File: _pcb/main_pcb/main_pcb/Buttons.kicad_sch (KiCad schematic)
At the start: 9 parts, among them SW1 SW_Push, SW2 SW_Push, SW3 SW_Push, SW4 SW_Push, SW5 SW_Push, SW6 SW_Push, SW7 SW_Push, SW8 SW_Push, U3 PCF8575DBR

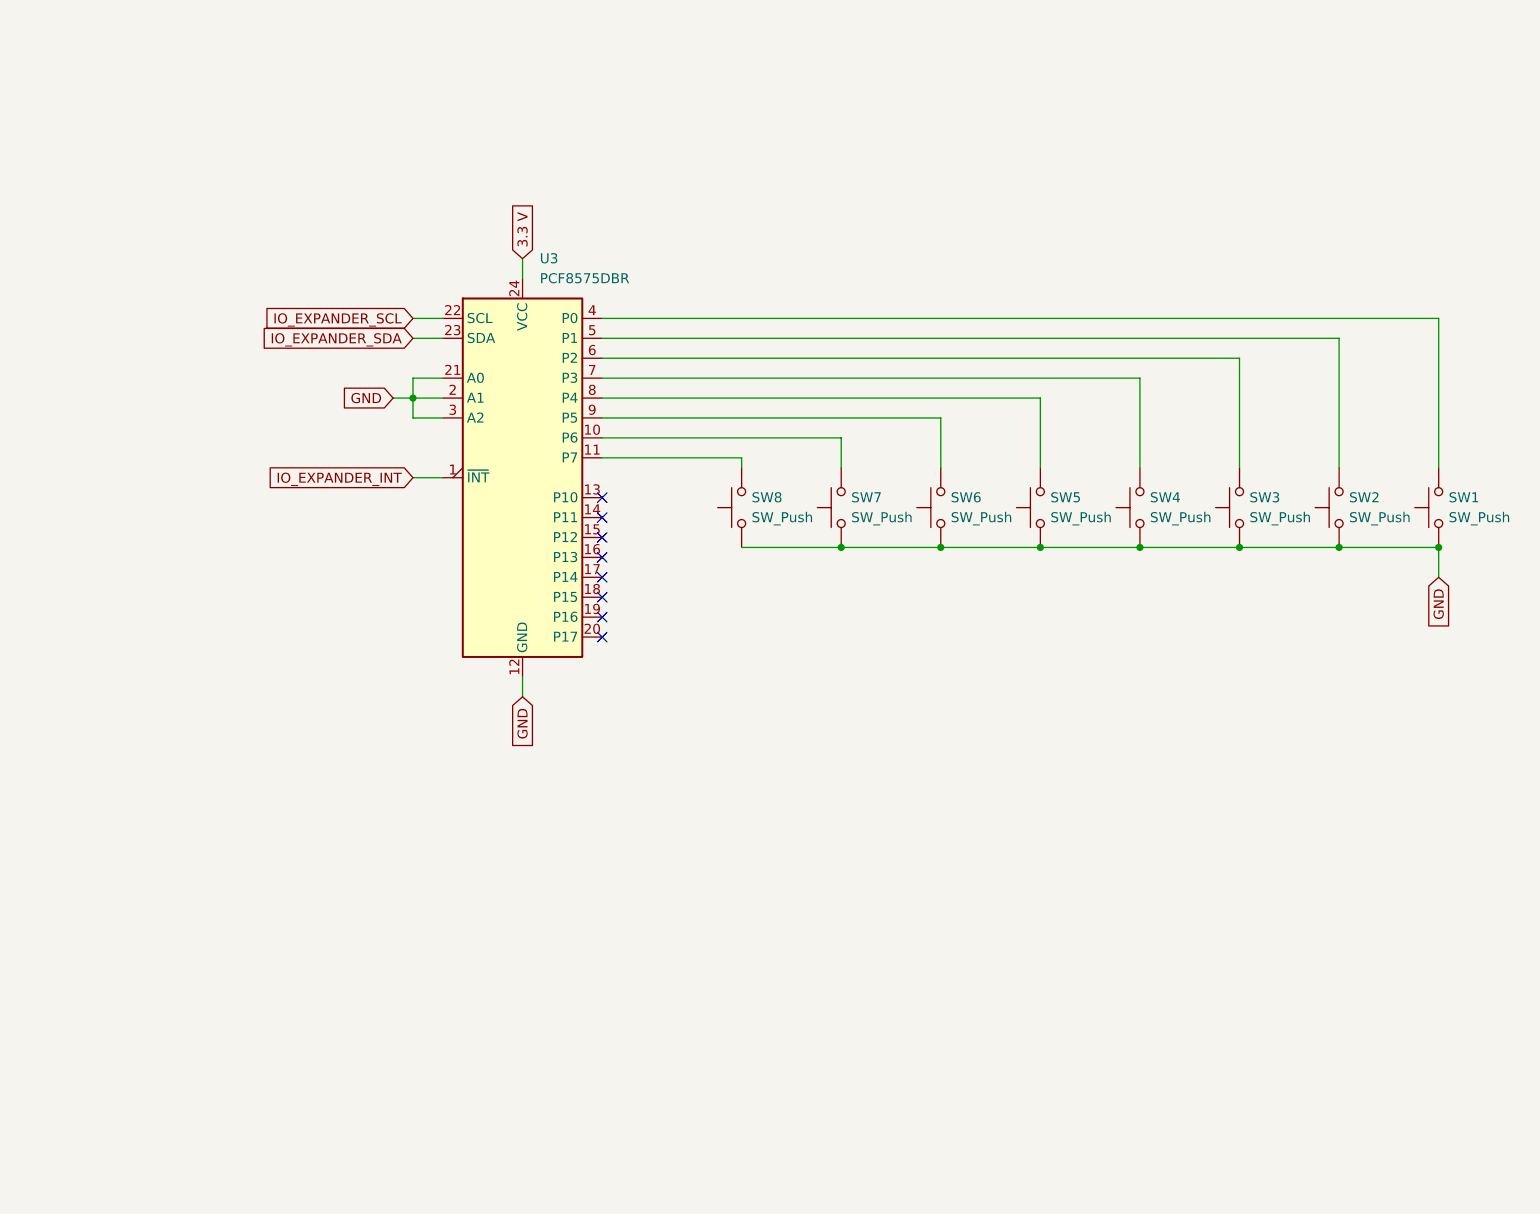
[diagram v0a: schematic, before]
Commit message: added leds to io expander
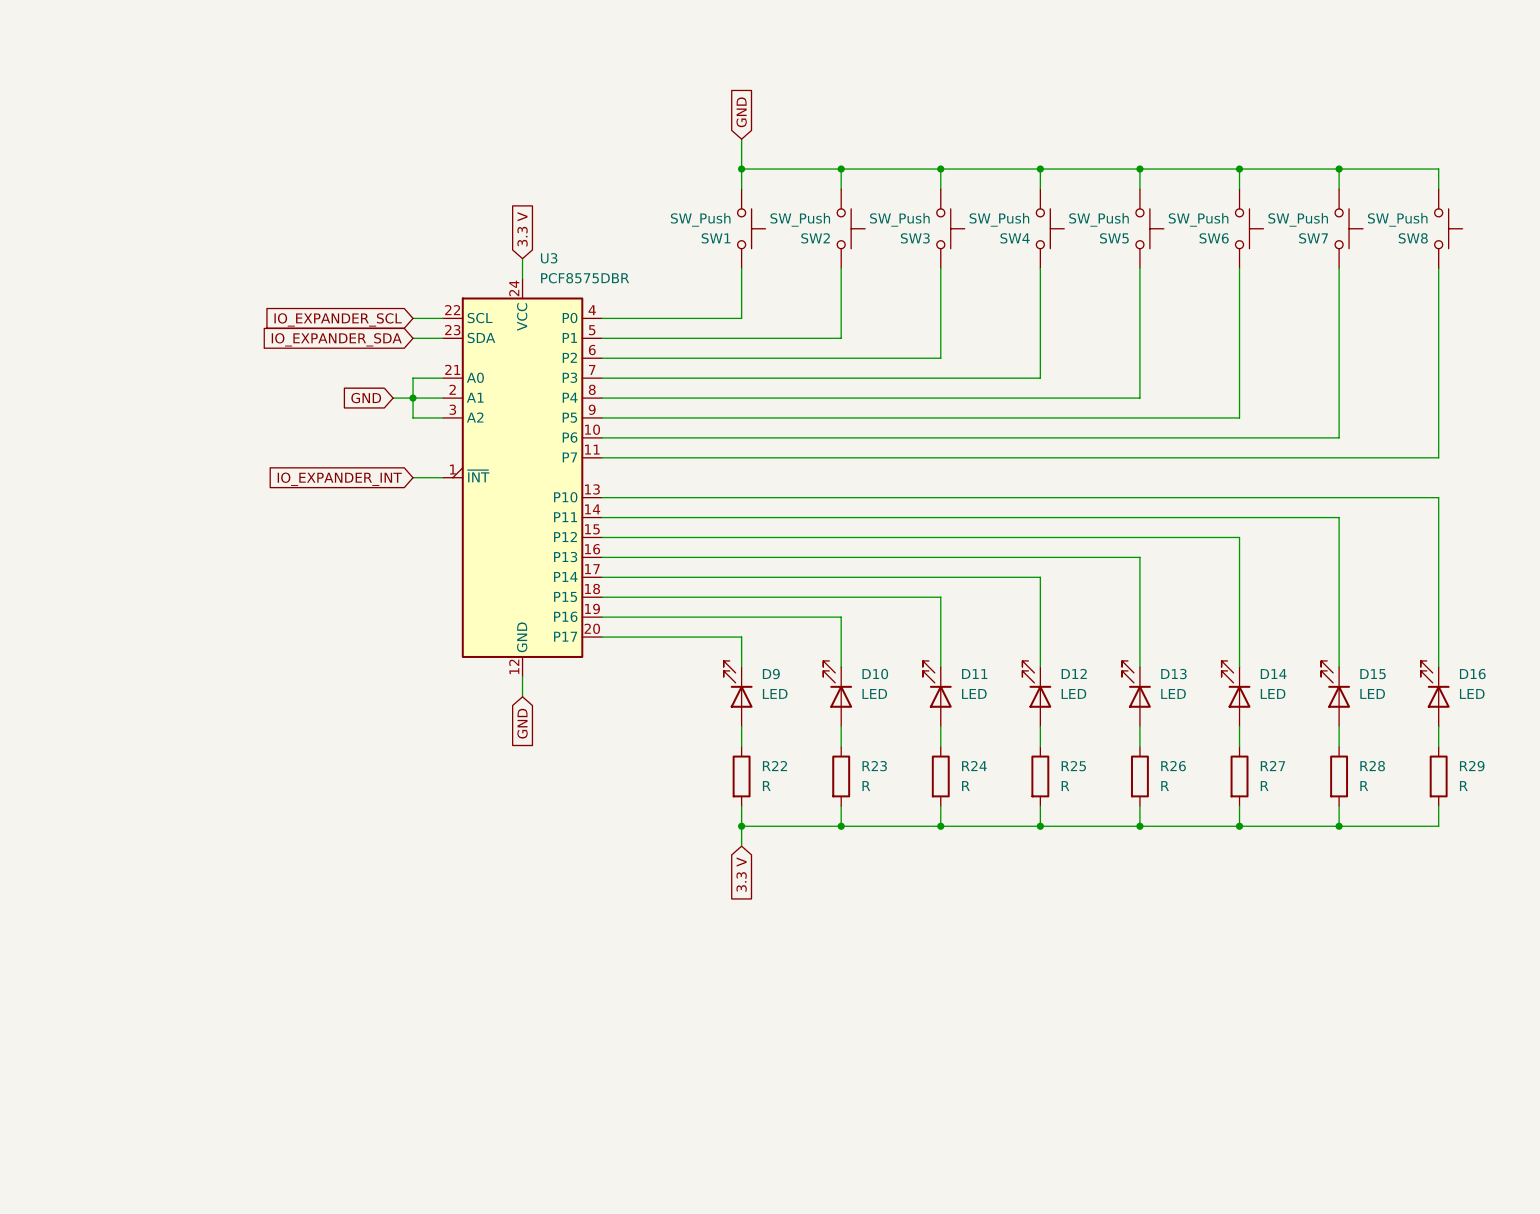
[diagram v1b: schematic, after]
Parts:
- added D10, D11, D12, D13, D14, D15, D16, D9: LED, symbol Device:LED
- added R22, R23, R24, R25, R26, R27, R28, R29: R, symbol Device:R
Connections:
- net 3.3 V: now also R22.2, R23.2, R24.2, R25.2, R26.2, R27.2, R28.2, R29.2
- net at U3.13 (P10): now also D16.1 (K)
- net at U3.14 (P11): now also D15.1 (K)
- net at U3.15 (P12): now also D14.1 (K)
- net at U3.16 (P13): now also D13.1 (K)
- net at U3.17 (P14): now also D12.1 (K)
- net at U3.18 (P15): now also D11.1 (K)
- net at U3.19 (P16): now also D10.1 (K)
- net at U3.20 (P17): now also D9.1 (K)
- new net: D12.2 (A), R25.1
- new net: D9.2 (A), R22.1
- new net: D14.2 (A), R27.1
- new net: D10.2 (A), R23.1
- new net: D13.2 (A), R26.1
- new net: D11.2 (A), R24.1
- new net: D16.2 (A), R29.1
- new net: D15.2 (A), R28.1
- no-connect marks 8 -> 0
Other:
- moved on the sheet: SW1, SW2, SW3, SW4, SW5, SW6, SW7, SW8

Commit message: moved to two pcf8574 instead of pcf8575
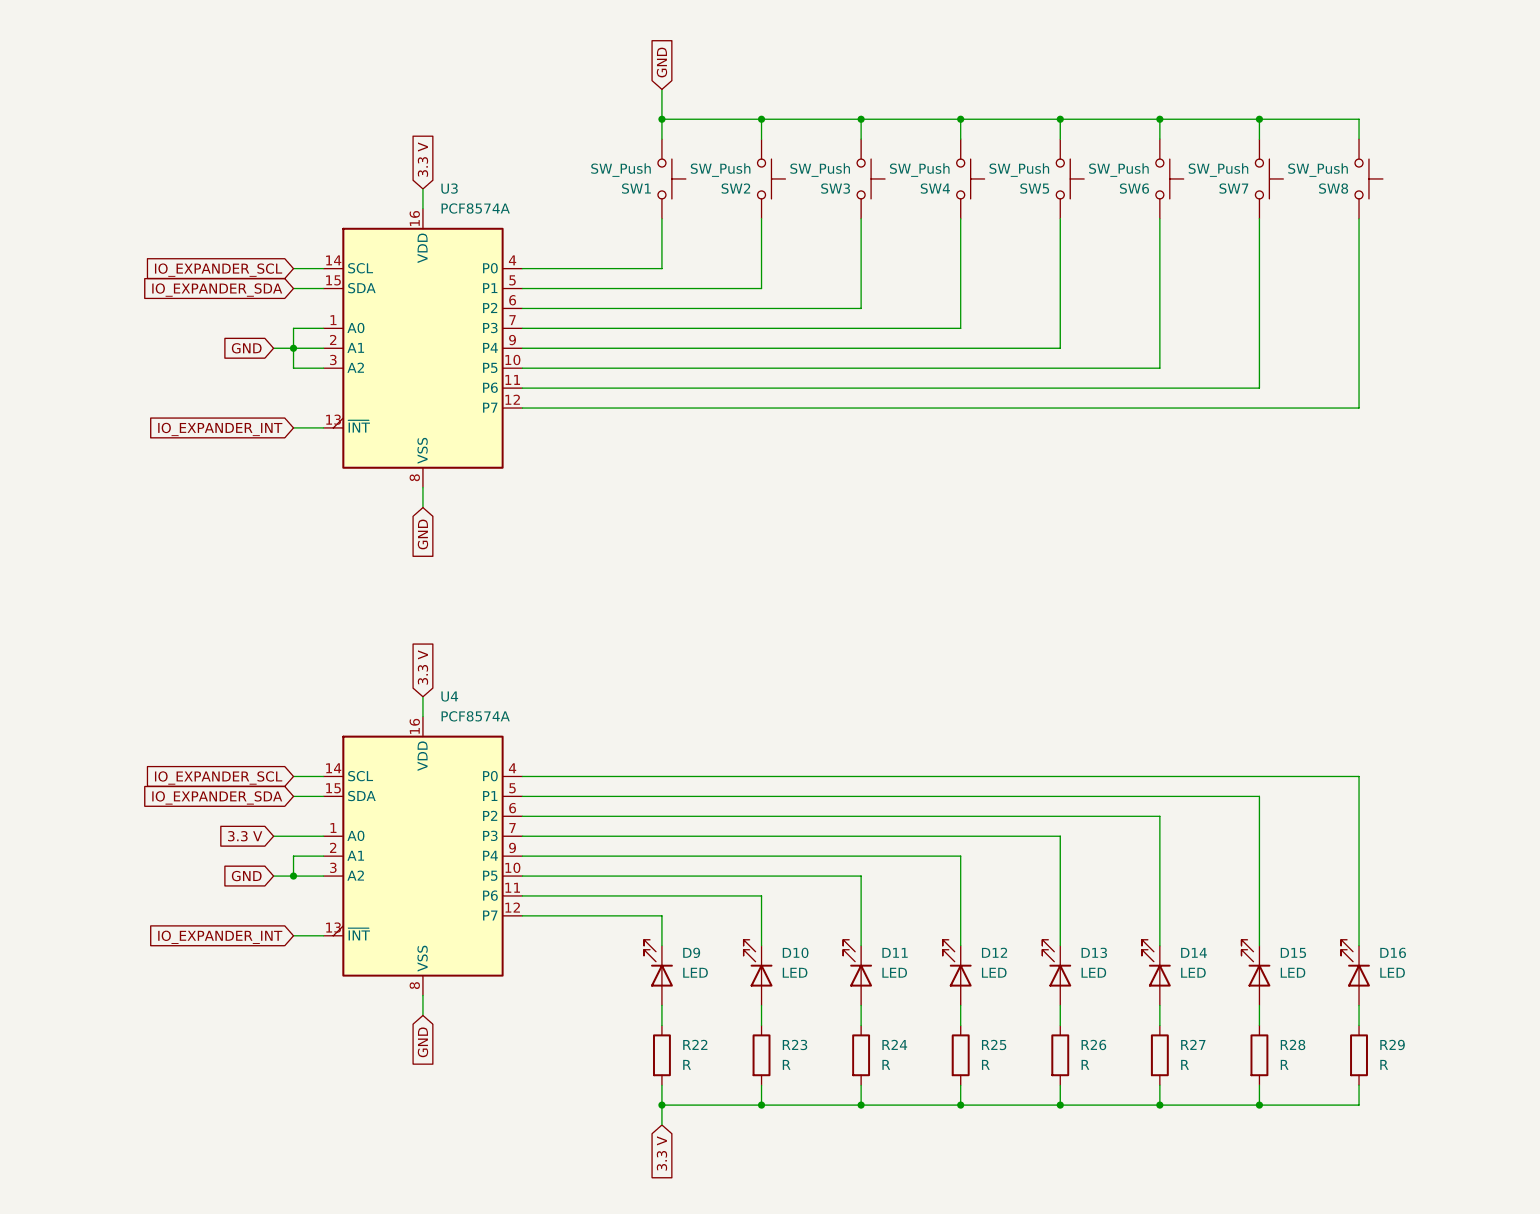
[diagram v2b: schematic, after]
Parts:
- removed U3: PCF8575DBR, Package_SO:SSOP-24_5.3x8.2mm_P0.65mm, symbol Interface_Expansion:PCF8575DBR
- added U3, U4: PCF8574A, Package_DIP:SMDIP-16_W9.53mm, symbol Interface_Expansion:PCF8574A
- D10, D11, D12, D13, D14, D15, D16, D9: footprint (none) -> LED_THT:LED_Rectangular_W3.9mm_H1.9mm
- R22, R23, R24, R25, R26, R27, R28, R29: footprint (none) -> Inductor_SMD:L_1206_3216Metric_Pad1.22x1.90mm_HandSolder
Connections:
- net 3.3 V: now also U3.16 (VDD), U4.1 (A0), U4.16 (VDD)
- net GND: now also U3.1 (A0), U3.2 (A1), U3.3 (A2), U3.8 (VSS), U4.2 (A1), U4.3 (A2), U4.8 (VSS)
- net IO_EXPANDER_INT: now also U3.13 (~{INT}), U4.13 (~{INT})
- net IO_EXPANDER_SCL: now also U3.14 (SCL), U4.14 (SCL)
- net IO_EXPANDER_SDA: now also U3.15 (SDA), U4.15 (SDA)
- net at SW1.2: now also U3.4 (P0)
- net at D12.1 (K): now also U4.9 (P4)
- net at D14.1 (K): now also U4.6 (P2)
- net at SW8.2: now also U3.12 (P7)
- net at D10.1 (K): now also U4.11 (P6)
- net at SW3.2: now also U3.6 (P2)
- net at D9.1 (K): now also U4.12 (P7)
- net at SW7.2: now also U3.11 (P6)
- net at D16.1 (K): now also U4.4 (P0)
- net at D15.1 (K): now also U4.5 (P1)
- net at D13.1 (K): now also U4.7 (P3)
- net at D11.1 (K): now also U4.10 (P5)
- net at SW2.2: now also U3.5 (P1)
- net at SW4.2: now also U3.7 (P3)
- net at SW5.2: now also U3.9 (P4)
- net at SW6.2: now also U3.10 (P5)
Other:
- moved on the sheet: D10, D11, D12, D13, D14, D15, D16, D9, R22, R23, R24, R25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

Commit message: both pcf an in and out
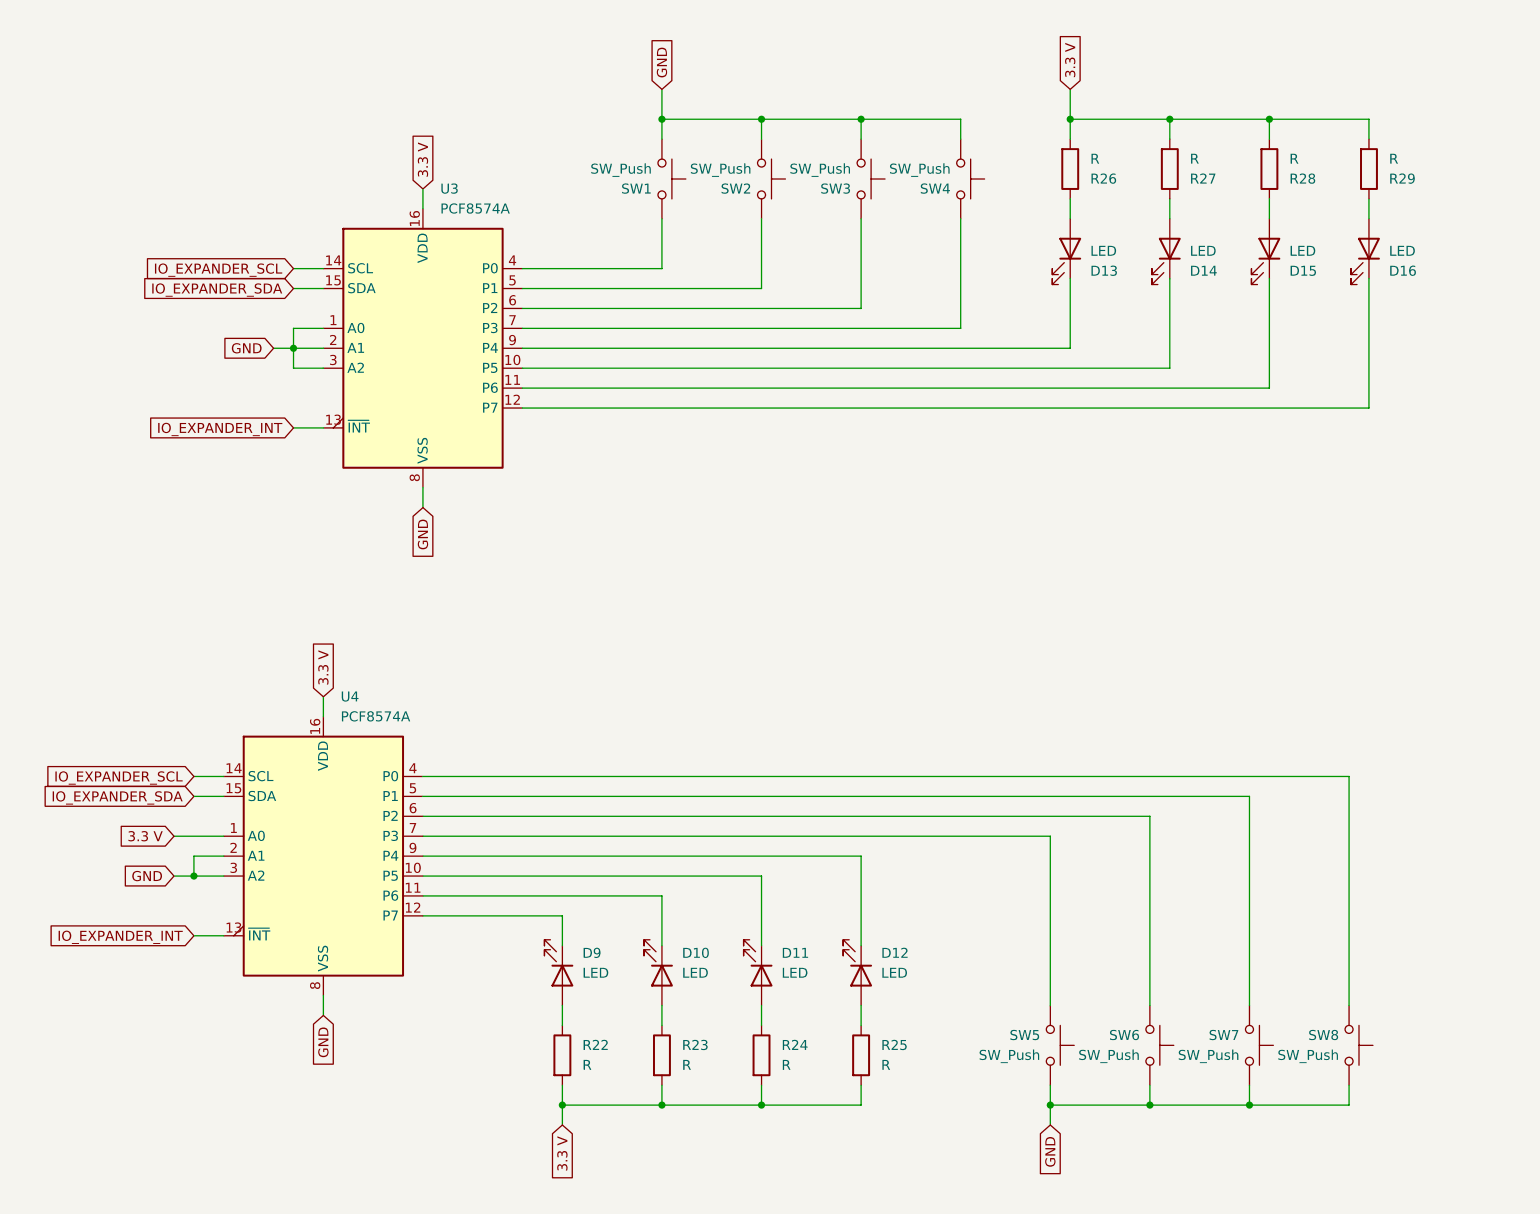
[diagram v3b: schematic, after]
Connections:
- net at D14.1 (K): now also U3.10 (P5); no longer U4.6 (P2)
- net at SW8.2: now also U4.4 (P0); no longer U3.12 (P7)
- net at SW6.2: now also U4.6 (P2); no longer U3.10 (P5)
- net at U3.11 (P6): now also D15.1 (K); no longer SW7.2
- net at U3.9 (P4): now also D13.1 (K); no longer SW5.2
- net at U4.7 (P3): now also SW5.2; no longer D13.1 (K)
- net at U4.5 (P1): now also SW7.2; no longer D15.1 (K)
- net at D16.1 (K): now also U3.12 (P7); no longer U4.4 (P0)
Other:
- moved on the sheet: D10, D11, D12, D13, D14, D15, D16, D9, R22, R23, R24, R25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

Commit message: changed ICs to THT
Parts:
- U3, U4: footprint Package_DIP:SMDIP-16_W9.53mm -> Package_DIP:DIP-16_W7.62mm
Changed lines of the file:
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@@
 			)
 		)
-		(property "Footprint" "Package_DIP:SMDIP-16_W9.53mm"
+		(property "Footprint" "Package_DIP:DIP-16_W7.62mm"
 			(at 86.36 60.96 0)
 			(effects
@@
 			)
 		)
-		(property "Footprint" "Package_DIP:SMDIP-16_W9.53mm"
+		(property "Footprint" "Package_DIP:DIP-16_W7.62mm"
 			(at 73.66 125.73 0)
 			(effects

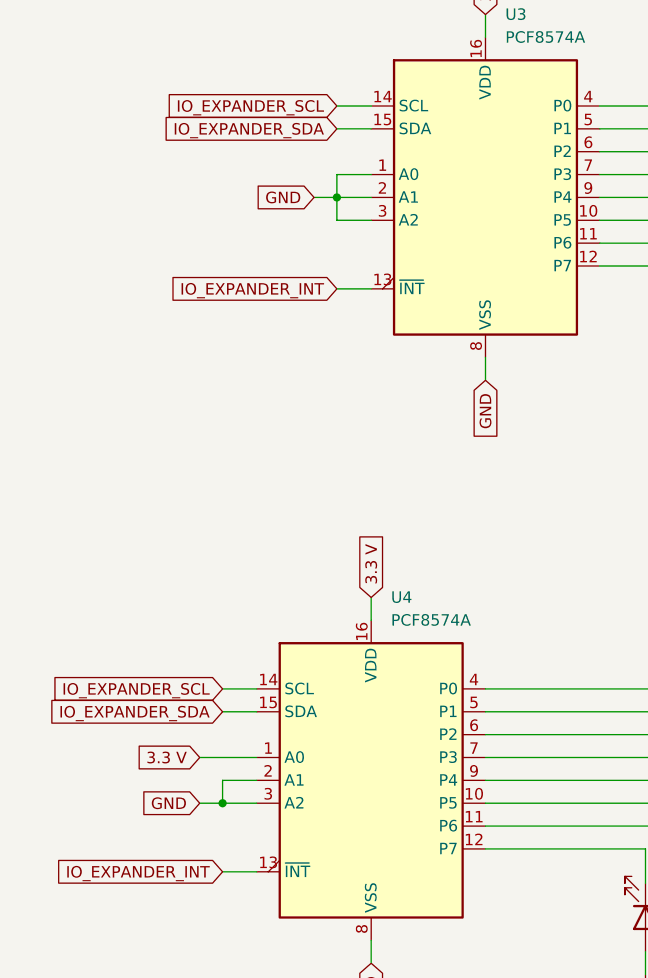
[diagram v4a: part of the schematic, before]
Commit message: switches the i2c addresses so that its better on pcb
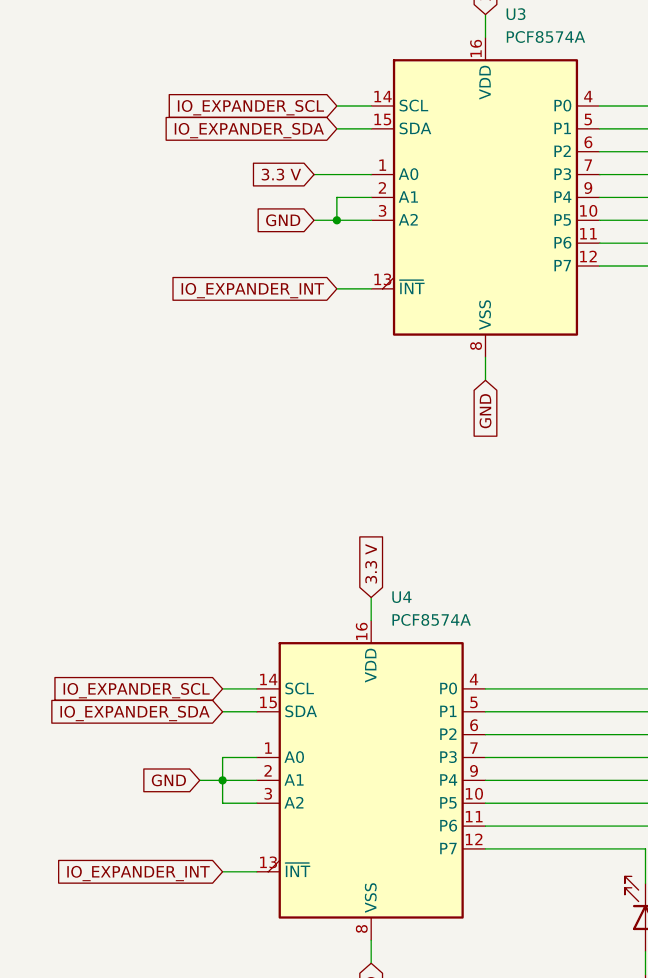
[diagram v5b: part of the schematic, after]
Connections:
- net 3.3 V: now also U3.1 (A0); no longer U4.1 (A0)
- net GND: now also U4.1 (A0); no longer U3.1 (A0)
